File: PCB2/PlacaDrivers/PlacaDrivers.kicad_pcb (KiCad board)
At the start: 2 copper layers, 0 parts

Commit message: Placa driver casi enrutada, step y medidas exportadas
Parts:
- added C10: 100nF, Capacitors_SMD:C_0805, F.Cu at (182.1, 47.8)
- added C11: 4.7uF, Capacitors_SMD:C_0805, F.Cu at (124.3, 131.4)
- added C12: 4.7uF, Capacitors_SMD:C_0805, F.Cu at (180.0, 47.8)
- added C15: 100nF, Capacitors_SMD:C_0805, F.Cu at (186.9, 70.4)
- added C16: 100nF, Capacitors_SMD:C_0805, F.Cu at (117.7, 109.3)
- added C17: 10uF, Capacitors_SMD:C_0805, F.Cu at (150.4, 80.5)
- added C18: 47uF, Capacitors_SMD:c_elec_6.3x4.5, F.Cu at (183.8, 63.8)
- added C19: 47uF, Capacitors_SMD:c_elec_6.3x4.5, F.Cu at (120.5, 114.1)
- added C20: 100nF, Capacitors_SMD:C_0805, F.Cu at (186.9, 68.6)
- added C21: 100nF, Capacitors_SMD:C_0805, F.Cu at (117.7, 107.3)
- added C22: 100nF, Capacitors_SMD:C_0805, F.Cu at (182.1, 72.9)
- added C23: 100nF, Capacitors_SMD:C_0805, F.Cu at (122.3, 106.5)
- added C24: 4.7uF, Capacitors_SMD:C_0805, F.Cu at (180.0, 72.9)
- added C25: 4.7uF, Capacitors_SMD:C_0805, F.Cu at (124.3, 106.5)
- added C28: 100nF, Capacitors_SMD:C_0805, F.Cu at (117.7, 82.1)
- added C29: 100nF, Capacitors_SMD:C_0805, F.Cu at (186.9, 95.3)
- added C3: 100nF, Capacitors_SMD:C_0805, F.Cu at (128.5, 133.9)
- added C30: 47uF, Capacitors_SMD:c_elec_6.3x4.5, F.Cu at (120.5, 89.0)
- added C31: 47uF, Capacitors_SMD:c_elec_6.3x4.5, F.Cu at (183.8, 88.2)
- added C32: 100nF, Capacitors_SMD:C_0805, F.Cu at (117.7, 84.2)
- added C33: 100nF, Capacitors_SMD:C_0805, F.Cu at (186.9, 93.2)
- added C34: 100nF, Capacitors_SMD:C_0805, F.Cu at (122.4, 81.1)
- added C35: 100nF, Capacitors_SMD:C_0805, F.Cu at (182.1, 97.8)
- added C36: 4.7uF, Capacitors_SMD:C_0805, F.Cu at (124.4, 81.1)
- added C37: 4.7uF, Capacitors_SMD:C_0805, F.Cu at (180.0, 97.8)
- added C4: 100nF, Capacitors_SMD:C_0805, F.Cu at (176.8, 45.4)
- added C40: 100nF, Capacitors_SMD:C_0805, F.Cu at (117.7, 56.5)
- added C41: 100nF, Capacitors_SMD:C_0805, F.Cu at (186.8, 117.9)
- added C42: 47uF, Capacitors_SMD:c_elec_6.3x4.5, F.Cu at (120.5, 63.1)
- added C43: 47uF, Capacitors_SMD:c_elec_6.3x4.5, F.Cu at (183.8, 113.1)
- added C44: 100nF, Capacitors_SMD:C_0805, F.Cu at (117.7, 58.5)
- added C45: 100nF, Capacitors_SMD:C_0805, F.Cu at (186.8, 119.8)
- added C46: 100nF, Capacitors_SMD:C_0805, F.Cu at (122.5, 56.2)
- added C47: 100nF, Capacitors_SMD:C_0805, F.Cu at (182.1, 121.2)
- added C48: 4.7uF, Capacitors_SMD:C_0805, F.Cu at (124.6, 56.2)
- added C49: 4.7uF, Capacitors_SMD:C_0805, F.Cu at (180.2, 121.2)
- added C5: 47uF, Capacitors_SMD:c_elec_6.3x4.5, F.Cu at (133.2, 132.2)
- added C6: 47uF, Capacitors_SMD:c_elec_6.3x4.5, F.Cu at (169.9, 48.4)
- added C7: 100nF, Capacitors_SMD:C_0805, F.Cu at (126.4, 133.9)
- added C8: 100nF, Capacitors_SMD:C_0805, F.Cu at (174.7, 45.4)
- added C9: 100nF, Capacitors_SMD:C_0805, F.Cu at (122.3, 131.4)
- added D1: MMSZ4700-G3-08, Diode_SMD:D_SOD-123, F.Cu at (160.5, 119.0)
- added JP1: SJ-A0, Jumpers:SMT-JUMPER_2_NO_SILK, F.Cu at (147.2, 86.9)
- added JP2: SJ-A1, Jumpers:SMT-JUMPER_2_NO_SILK, F.Cu at (149.1, 86.9)
- added JP3: SJ-A2, Jumpers:SMT-JUMPER_2_NO_SILK, F.Cu at (151.0, 86.9)
- added JP4: SJ-A3, Jumpers:SMT-JUMPER_2_NO_SILK, F.Cu at (152.9, 86.9)
- added JP5: SJ-A4, Jumpers:SMT-JUMPER_2_NO_SILK, F.Cu at (154.7, 86.9)
- added JP6: SJ-A5, Jumpers:SMT-JUMPER_2_NO_SILK, F.Cu at (156.6, 86.9)
- added P1: MOTOR_5, Connectors_Molex:Molex_Microfit3_Header_02x01_Angled_43045-020x, F.Cu at (103.7, 126.1)
- added P10: MOTOR_3, Connectors_Molex:Molex_Microfit3_Header_02x01_Angled_43045-020x, F.Cu at (200.6, 100.9)
- added P11: MOTOR_8, Connectors_Molex:Molex_Microfit3_Header_02x01_Angled_43045-020x, F.Cu at (103.7, 50.4)
- added P12: MOTOR_4, Connectors_Molex:Molex_Microfit3_Header_02x01_Angled_43045-020x, F.Cu at (200.9, 126.5)
- added P2: MOTOR_1, Connectors_Molex:Molex_Microfit3_Header_02x01_Angled_43045-020x, F.Cu at (200.9, 50.3)
- added P3: MOTOR_2, Connectors_Molex:Molex_Microfit3_Header_02x01_Angled_43045-020x, F.Cu at (200.9, 75.7)
- added P4: MOTOR_6, Connectors_Molex:Molex_Microfit3_Header_02x01_Angled_43045-020x, F.Cu at (103.7, 101.2)
- added P5: HEADER1, Pin_Headers:Pin_Header_Straight_1x15, F.Cu at (131.2, 64.2)
- added P6: HEADER2, Pin_Headers:Pin_Header_Straight_1x15, F.Cu at (172.8, 64.2)
- added P7: MAIN POWER, Connectors_Molex:Molex_Microfit3_Header_02x02_Angled_43045-040x, F.Cu at (154.3, 129.3)
- added P9: MOTOR_7, Connectors_Molex:Molex_Microfit3_Header_02x01_Angled_43045-020x, F.Cu at (103.7, 75.8)
- added Q1: FDD9411L-F085, TO_SOT_Packages_SMD:TO-252-3_TabPin4, F.Cu at (152.4, 120.2)
- added R1: 20k, Resistors_SMD:R_0603, F.Cu at (159.7, 122.6)
- added R10: 1k, Resistors_SMD:R_0603, F.Cu at (180.3, 53.7)
- added R100: 1k, Resistors_SMD:R_0603, F.Cu at (124.3, 48.9)
- added R101: 1k, Resistors_SMD:R_0603, F.Cu at (124.3, 45.8)
- added R102: 1k, Resistors_SMD:R_0603, F.Cu at (180.5, 126.9)
- added R103: 1k, Resistors_SMD:R_0603, F.Cu at (180.5, 131.5)
- added R104: 1, Resistors_SMD:R_0603, F.Cu at (124.3, 53.4)
- added R105: 1, Resistors_SMD:R_0603, F.Cu at (180.5, 123.9)
- added R11: 1k, Resistors_SMD:R_0603, F.Cu at (180.3, 56.8)
- added R13: 1k, Resistors_SMD:R_0603, F.Cu at (123.8, 127.1)
- added R15: 1k, Resistors_SMD:R_0603, F.Cu at (123.8, 124.1)
- added R16: 1k, Resistors_SMD:R_0603, F.Cu at (123.8, 121.0)
- added R17: 1k, Resistors_SMD:R_0603, F.Cu at (180.3, 55.2)
- added R18: 1k, Resistors_SMD:R_0603, F.Cu at (180.3, 58.3)
- added R19: 1, Resistors_SMD:R_0603, F.Cu at (123.8, 128.6)
- added R2: 1k, Resistors_SMD:R_0603, F.Cu at (180.3, 52.1)
- added R20: 1, Resistors_SMD:R_0603, F.Cu at (180.3, 50.6)
- added R21: 10k, Resistors_SMD:R_0603, F.Cu at (156.7, 84.4)
- added R22: 10k, Resistors_SMD:R_0603, F.Cu at (154.8, 84.4)
- added R23: 10k, Resistors_SMD:R_0603, F.Cu at (152.9, 84.4)
- added R24: 10k, Resistors_SMD:R_0603, F.Cu at (151.0, 84.4)
- added R25: 10k, Resistors_SMD:R_0603, F.Cu at (149.1, 84.4)
- added R26: 10k, Resistors_SMD:R_0603, F.Cu at (147.2, 84.3)
- added R33: 1k, Resistors_SMD:R_0603, F.Cu at (180.3, 78.5)
- added R34: 1k, Resistors_SMD:R_0603, F.Cu at (180.3, 81.5)
- added R36: 1k, Resistors_SMD:R_0603, F.Cu at (124.1, 100.7)
- added R37: 1k, Resistors_SMD:R_0603, F.Cu at (124.1, 97.8)
- added R39: 1k, Resistors_SMD:R_0603, F.Cu at (180.3, 77.0)
- added R40: 1k, Resistors_SMD:R_0603, F.Cu at (124.1, 102.2)
- added R41: 1k, Resistors_SMD:R_0603, F.Cu at (180.3, 80.0)
- added R42: 1k, Resistors_SMD:R_0603, F.Cu at (180.3, 83.0)
- added R43: 1k, Resistors_SMD:R_0603, F.Cu at (124.1, 99.3)
- added R44: 1k, Resistors_SMD:R_0603, F.Cu at (124.1, 96.2)
- added R45: 10k, Resistors_SMD:R_0603, F.Cu at (146.0, 79.5)
- added R46: 1, Resistors_SMD:R_0603, F.Cu at (180.3, 75.5)
- added R47: 1, Resistors_SMD:R_0603, F.Cu at (124.1, 103.7)
- added R5: 220, Resistors_SMD:R_0603, F.Cu at (135.3, 87.8)
- added R7: 1k, Resistors_SMD:R_0603, F.Cu at (123.8, 125.6)
- added R70: 10k, Resistors_SMD:R_0603, F.Cu at (168.9, 79.4)
- added R71: 1k, Resistors_SMD:R_0603, F.Cu at (124.1, 75.3)
- added R72: 1k, Resistors_SMD:R_0603, F.Cu at (124.1, 72.2)
- added R74: 1k, Resistors_SMD:R_0603, F.Cu at (180.4, 103.4)
- added R75: 1k, Resistors_SMD:R_0603, F.Cu at (180.4, 106.5)
- added R77: 1k, Resistors_SMD:R_0603, F.Cu at (124.1, 76.8)
- added R78: 1k, Resistors_SMD:R_0603, F.Cu at (180.4, 101.9)
- added R79: 10k, Resistors_SMD:R_0603, F.Cu at (168.9, 82.0)
- added R8: 1k, Resistors_SMD:R_0603, F.Cu at (123.8, 122.5)
- added R80: 1k, Resistors_SMD:R_0603, F.Cu at (124.1, 73.8)
- added R81: 1k, Resistors_SMD:R_0603, F.Cu at (124.1, 70.8)
- added R82: 1k, Resistors_SMD:R_0603, F.Cu at (180.4, 105.0)
- added R83: 1k, Resistors_SMD:R_0603, F.Cu at (180.4, 108.0)
- added R84: 1, Resistors_SMD:R_0603, F.Cu at (124.1, 78.3)
- added R85: 1, Resistors_SMD:R_0603, F.Cu at (180.4, 100.4)
- added R9: 10k, Resistors_SMD:R_0603, F.Cu at (135.3, 90.6)
- added R92: 1k, Resistors_SMD:R_0603, F.Cu at (124.3, 50.4)
- added R93: 1k, Resistors_SMD:R_0603, F.Cu at (124.3, 47.3)
- added R95: 1k, Resistors_SMD:R_0603, F.Cu at (180.5, 128.4)
- added R96: 1k, Resistors_SMD:R_0603, F.Cu at (180.5, 129.9)
- added R98: 1k, Resistors_SMD:R_0603, F.Cu at (124.3, 51.9)
- added R99: 1k, Resistors_SMD:R_0603, F.Cu at (180.5, 125.4)
- added REF**: MountingHole_3.2mm_M3, Mounting_Holes:MountingHole_3.2mm_M3, F.Cu at (194.8, 112.2)
- added REF**: MountingHole_3.2mm_M3, Mounting_Holes:MountingHole_3.2mm_M3, F.Cu at (104.8, 112.2)
- added REF**: MountingHole_3.2mm_M3, Mounting_Holes:MountingHole_3.2mm_M3, F.Cu at (194.8, 62.2)
- added REF**: MountingHole_3.2mm_M3, Mounting_Holes:MountingHole_3.2mm_M3, F.Cu at (104.8, 62.2)
- added U1: TB9051FTG, frizzy_ics:QFN-28-1EP_6x6mm_Pitch0.65mm, F.Cu at (187.7, 50.3)
- added U2: TB9051FTG, frizzy_ics:QFN-28-1EP_6x6mm_Pitch0.65mm, F.Cu at (187.7, 75.7)
- added U3: TB9051FTG, frizzy_ics:QFN-28-1EP_6x6mm_Pitch0.65mm, F.Cu at (187.7, 100.9)
- added U4: TB9051FTG, frizzy_ics:QFN-28-1EP_6x6mm_Pitch0.65mm, F.Cu at (187.7, 126.2)
- added U5: TB9051FTG, frizzy_ics:QFN-28-1EP_6x6mm_Pitch0.65mm, F.Cu at (116.7, 126.1)
- added U6: TB9051FTG, frizzy_ics:QFN-28-1EP_6x6mm_Pitch0.65mm, F.Cu at (116.7, 100.9)
- added U7: TB9051FTG, frizzy_ics:QFN-28-1EP_6x6mm_Pitch0.65mm, F.Cu at (116.7, 75.8)
- added U8: TB9051FTG, frizzy_ics:QFN-28-1EP_6x6mm_Pitch0.65mm, F.Cu at (116.7, 50.6)
- added U9: PCA9685, Silicon-Standard:TSSOP28, F.Cu at (152.5, 74.0)
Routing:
- net VIN: track 0.00 -> 543.1 mm, vias 0 -> 16
- net VCC: track 0.00 -> 364.3 mm, vias 0 -> 13
- net DIAG: track 0.00 -> 287.7 mm, vias 0 -> 13
- net ENB: track 0.00 -> 234.1 mm, vias 0 -> 14
- net EN: track 0.00 -> 228.5 mm, vias 0 -> 10
- net GND: track 0.00 -> 217.2 mm, vias 0 -> 170
- net PWM2_4: track 0.00 -> 77.3 mm, vias 0 -> 2
- net PWM1_4: track 0.00 -> 74.9 mm, vias 0 -> 2
- net PWM1_5: track 0.00 -> 69.8 mm, vias 0 -> 6
- net PWM2_5: track 0.00 -> 66.1 mm, vias 0 -> 4
- net PWM1_6: track 0.00 -> 52.6 mm, vias 0 -> 8
- net PWM2_6: track 0.00 -> 50.6 mm, vias 0 -> 8
- net PWM2_8: track 0.00 -> 44.2 mm
- net PWM1_8: track 0.00 -> 43.8 mm, vias 0 -> 2
- net PWM1_1: track 0.00 -> 37.9 mm, vias 0 -> 2
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- added copper zone on B.Cu, net GND
- added copper zone on F.Cu, net GND
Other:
- board outline added: 107.4 x 95.9 mm

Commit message: Placa enrutada
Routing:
- net PWM2_3: track 0.00 -> 53.3 mm, vias 0 -> 4
- net PWM1_3: track 0.00 -> 49.7 mm, vias 0 -> 4
- net PWM2_2: track 1.13 -> 45.6 mm, vias 1 -> 6
- net PWM1_2: track 7.67 -> 43.5 mm, vias 2 -> 6
- net SDA: track 3.24 -> 28.7 mm, vias 0 -> 3
- net SCL: track 3.24 -> 27.7 mm, vias 0 -> 3
- net GND: track 217.2 -> 222.2 mm, vias 170 -> 250
- net PWM1_1: track 37.9 -> 37.2 mm
- net A0: track 13.3 -> 13.8 mm
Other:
- board size 107.4 x 95.9 mm -> 116.6 x 95.9 mm

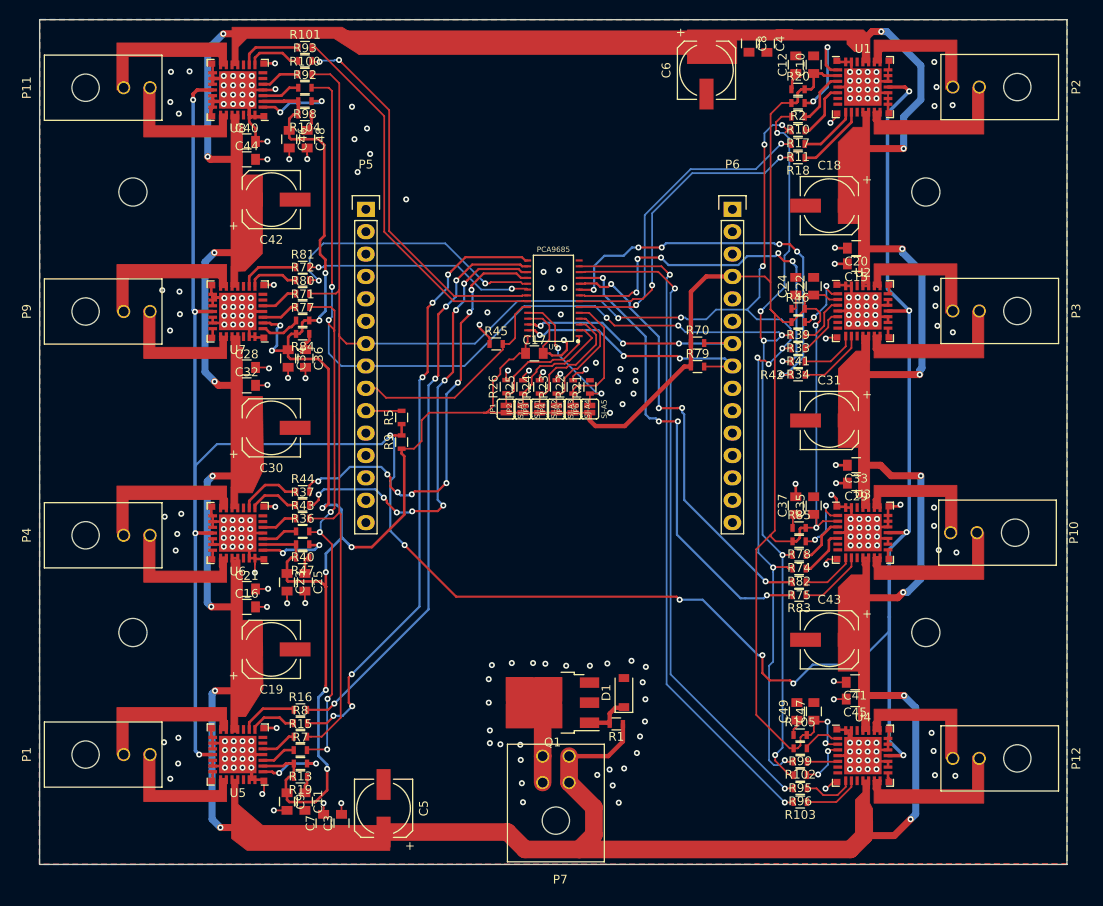
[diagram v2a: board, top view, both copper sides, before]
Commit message: Serigrafía colocada
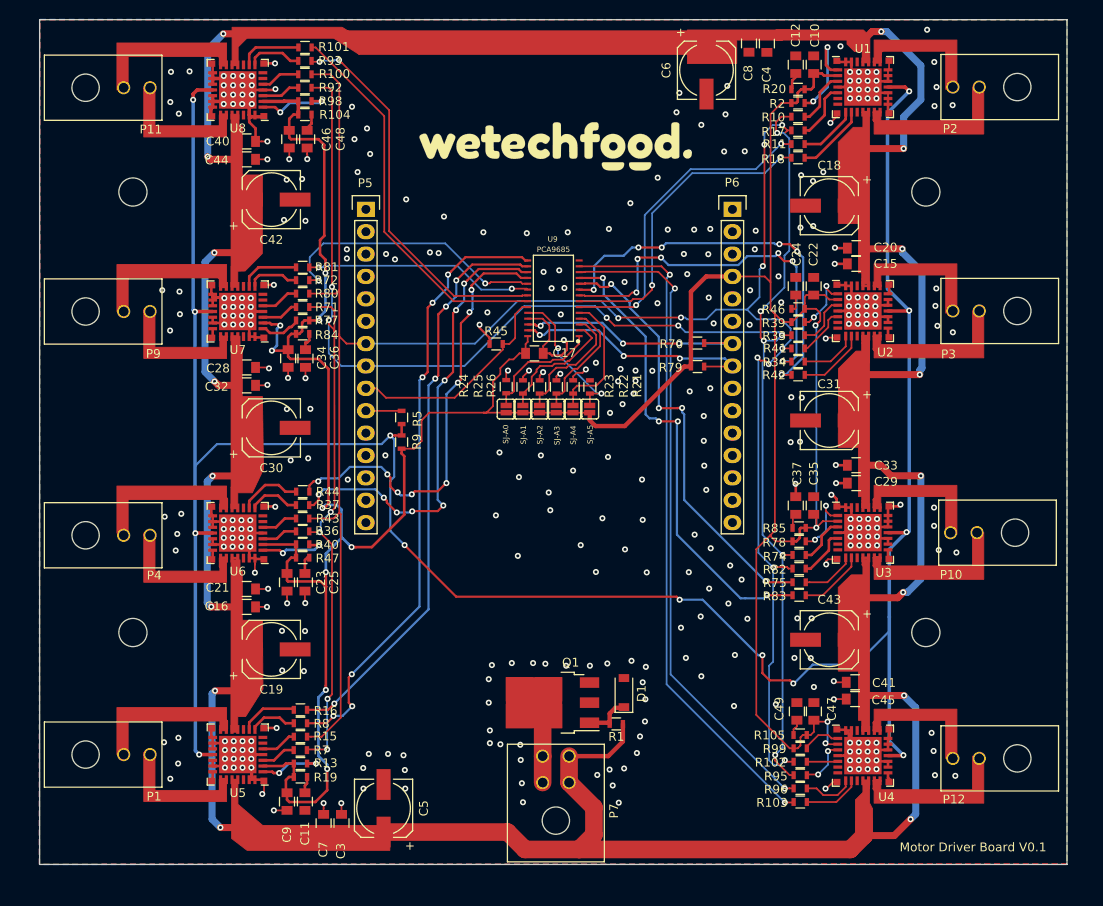
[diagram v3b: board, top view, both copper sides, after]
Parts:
- added G***: LOGO, logos_frizzy:logoWTF_small, F.Cu at (152.7, 57.0)
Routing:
- net GND: vias 250 -> 362
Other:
- board text added: "Motor Driver Board V0.1"

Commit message: Documentos de referencia actualizados
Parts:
- added G***: LOGO, logos_frizzy:cuadradoo, F.Cu at (206.5, 132.0)
- added G***: LOGO, logos_frizzy:cuadradoo, F.Cu at (206.5, 107.0)
- added G***: LOGO, logos_frizzy:cuadradoo, F.Cu at (206.5, 82.0)
- added G***: LOGO, logos_frizzy:cuadradoo, F.Cu at (206.5, 56.5)
- added G***: LOGO, logos_frizzy:cuadradoo, F.Cu at (102.8, 132.0)
- added G***: LOGO, logos_frizzy:cuadradoo, F.Cu at (102.8, 107.0)
- added G***: LOGO, logos_frizzy:cuadradoo, F.Cu at (102.8, 82.0)
- added G***: LOGO, logos_frizzy:cuadradoo, F.Cu at (102.8, 56.5)
- added REF**: MountingHole_3.2mm_M3, Mounting_Holes:MountingHole_3.2mm_M3, F.Cu at (172.5, 105.8)
- added REF**: MountingHole_3.2mm_M3, Mounting_Holes:MountingHole_3.2mm_M3, F.Cu at (131.5, 58.8)
- added REF**: MountingHole_3.2mm_M3, Mounting_Holes:MountingHole_3.2mm_M3, F.Cu at (172.5, 58.8)
- added REF**: MountingHole_3.2mm_M3, Mounting_Holes:MountingHole_3.2mm_M3, F.Cu at (131.5, 105.8)
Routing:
- net PWM1_3: track 49.7 -> 56.6 mm
- net PWM2_3: track 53.3 -> 56.6 mm
- net PWM1_1: track 37.2 -> 38.0 mm
- net PWM2_2: track 45.6 -> 46.2 mm
- net GND: vias 362 -> 353
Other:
- board size 116.6 x 95.9 mm -> 117 x 96 mm
- board text added: "+"
- board text added: "MOTOR:"
